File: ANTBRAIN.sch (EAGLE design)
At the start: 26 parts, among them IC1 ATMEGA328P, SW1 SWITCH-SPDTB

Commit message: Shrunk board to 36x36mm
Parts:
- H4: value ICSP -> ICSP2X3-2MM; device pinhead:PINHD-2X3 -> freetronics-jon:ICSP2X3-2MM
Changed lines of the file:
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@@
 <part name="U$5" library="SparkFun" deviceset="5V" device=""/>
 <part name="C6" library="freetronics-master-v1.1" deviceset="CAP" device="0603" value="100nF"/>
-<part name="H4" library="pinhead" deviceset="PINHD-2X3" device="" value="ICSP"/>
 <part name="GND22" library="SparkFun" deviceset="GND" device=""/>
 <part name="U$12" library="SparkFun" deviceset="5V" device=""/>
@@
 <part name="C9" library="freetronics-jon" deviceset="CAP" device="0805" value="10uF"/>
 <part name="U$9" library="SparkFun" deviceset="5V" device=""/>
+<part name="H4" library="freetronics-jon" deviceset="ICSP" device="2X3-2MM"/>
 </parts>
 <sheets>
@@
 <attribute name="VALUE" x="151.384" y="173.101" size="1.778" layer="96"/>
 </instance>
-<instance part="H4" gate="A" x="170.18" y="71.12"/>
 <instance part="GND22" gate="1" x="193.04" y="66.04"/>
 <instance part="U$12" gate="G$1" x="193.04" y="73.66"/>
@@
 </instance>
 <instance part="U$9" gate="G$1" x="215.9" y="76.2"/>
+<instance part="H4" gate="G$1" x="170.18" y="71.12"/>
 </instances>
 <busses>
@@
 </segment>
 <segment>
-<wire x1="175.26" y1="68.58" x2="193.04" y2="68.58" width="0.1524" layer="91"/>
-<pinref part="H4" gate="A" pin="6"/>
+<wire x1="180.34" y1="68.58" x2="193.04" y2="68.58" width="0.1524" layer="91"/>
 <pinref part="GND22" gate="1" pin="GND"/>
 <label x="182.88" y="68.58" size="1.778" layer="95"/>
+<pinref part="H4" gate="G$1" pin="6"/>
 </segment>
 <segment>
@@
 </segment>
 <segment>
-<wire x1="175.26" y1="73.66" x2="193.04" y2="73.66" width="0.1524" layer="91"/>
-<pinref part="H4" gate="A" pin="2"/>
+<wire x1="180.34" y1="73.66" x2="193.04" y2="73.66" width="0.1524" layer="91"/>
 <pinref part="U$12" gate="G$1" pin="5V"/>
 <label x="182.88" y="73.66" size="1.778" layer="95"/>
+<pinref part="H4" gate="G$1" pin="2"/>
 </segment>
 <segment>
@@
 </segment>
 <segment>
-<wire x1="167.64" y1="68.58" x2="147.32" y2="68.58" width="0.1524" layer="91"/>
-<pinref part="H4" gate="A" pin="5"/>
+<wire x1="160.02" y1="68.58" x2="147.32" y2="68.58" width="0.1524" layer="91"/>
 <label x="149.86" y="68.58" size="1.778" layer="95"/>
+<pinref part="H4" gate="G$1" pin="5"/>
 </segment>
 <segment>
@@
 </segment>
 <segment>
-<wire x1="167.64" y1="71.12" x2="147.32" y2="71.12" width="0.1524" layer="91"/>
-<pinref part="H4" gate="A" pin="3"/>
+<wire x1="160.02" y1="71.12" x2="147.32" y2="71.12" width="0.1524" layer="91"/>
 <label x="149.86" y="71.12" size="1.778" layer="95"/>
+<pinref part="H4" gate="G$1" pin="3"/>
 </segment>
 </net>
@@
 </segment>
 <segment>
-<wire x1="167.64" y1="73.66" x2="147.32" y2="73.66" width="0.1524" layer="91"/>
-<pinref part="H4" gate="A" pin="1"/>
+<wire x1="160.02" y1="73.66" x2="147.32" y2="73.66" width="0.1524" layer="91"/>
 <label x="149.86" y="73.66" size="1.778" layer="95"/>
+<pinref part="H4" gate="G$1" pin="1"/>
 </segment>
 </net>
@@
 </segment>
 <segment>
-<wire x1="175.26" y1="71.12" x2="193.04" y2="71.12" width="0.1524" layer="91"/>
-<pinref part="H4" gate="A" pin="4"/>
+<wire x1="180.34" y1="71.12" x2="193.04" y2="71.12" width="0.1524" layer="91"/>
 <label x="182.88" y="71.12" size="1.778" layer="95"/>
-</segment>
-</net>
+<pinref part="H4" gate="G$1" pin="4"/>
+</segment>
+</net>

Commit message: Finished routing for v1.0 release
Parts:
- removed U$2, U$6: L9110SO8, freetronics-jon:L9110SO8
- added IC2, IC3: L9110SO8, freetronics-jon:L9110SO8
- added JP10: POWER, freetronics-jon:M022MM
- added JP8: (no value), freetronics-jon:M022MM
- added JP9: D13, freetronics-jon:M022MM
- added LED2: RED, freetronics-jon:LED0603
- added R2, R3: 10K, freetronics-jon:RESISTOR0603
- added R4: 1K, freetronics-jon:RESISTOR0603
- added R6, R7: 470R, freetronics-jon:RESISTOR0603
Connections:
- removed net N$1: JP2.1, U$2.B
- removed net N$2: JP2.2, U$2.A
- removed net N$3: JP5.2, U$6.B
- removed net N$4: JP5.1, U$6.A
- new net LA: IC2.A, JP2.2
- new net LB: IC2.B, JP2.1
- new net N$5: LED2.A, R4.1
- new net N$6: JP10.1, R7.1
- new net N$8: JP9.1, R6.1
- new net RA: IC3.A, JP5.1
- new net RB: IC3.B, JP5.2
- net 5V: now also R7.2
- net A6: now also R2.2, R3.1
- net D10: now also IC3.OB; no longer U$6.OB
- net D13_SCK: now also R4.2, R6.2
- net D7: now also IC2.OA; no longer U$2.OA
- net D8: now also IC2.OB; no longer U$2.OB
- net D9: now also IC3.OA; no longer U$6.OA
- net GND: now also IC2.GND, IC3.GND, JP10.2, JP9.2, LED2.C, R2.1; no longer U$2.GND, U$6.GND
- net N$9: now also JP8.2
- net VBAT: now also IC2.VCC, IC3.VCC, JP8.1, R3.2; no longer U$2.VCC, U$6.VCC
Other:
- note added: "External LEDs"
- note added: "Flysky Receiver"
- note added: "H-Bridges"
- note added: "Power Supply"
- note added: "https://www.banggood.com/IRangX-Tiny-2_4G-6CH-Flysk-Receiver-Compatible-with-Flysky-PPM-Output-for-Eachine-QX80-QX90-QX95-p-1089802.html"
- note removed: "Front servo control Filter caps https://www.banggood.com/IRangX-Tiny-2_4G-6CH-Flysk-Receiver-Compatible-with-Flysky-PPM-Output-for-Eachine-QX80-QX90-QX95-p-1089802.html"
- moved on the sheet: C2, C3, C6, C8, C9, H3, JP1, JP2, JP3, JP4, JP5, JP7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

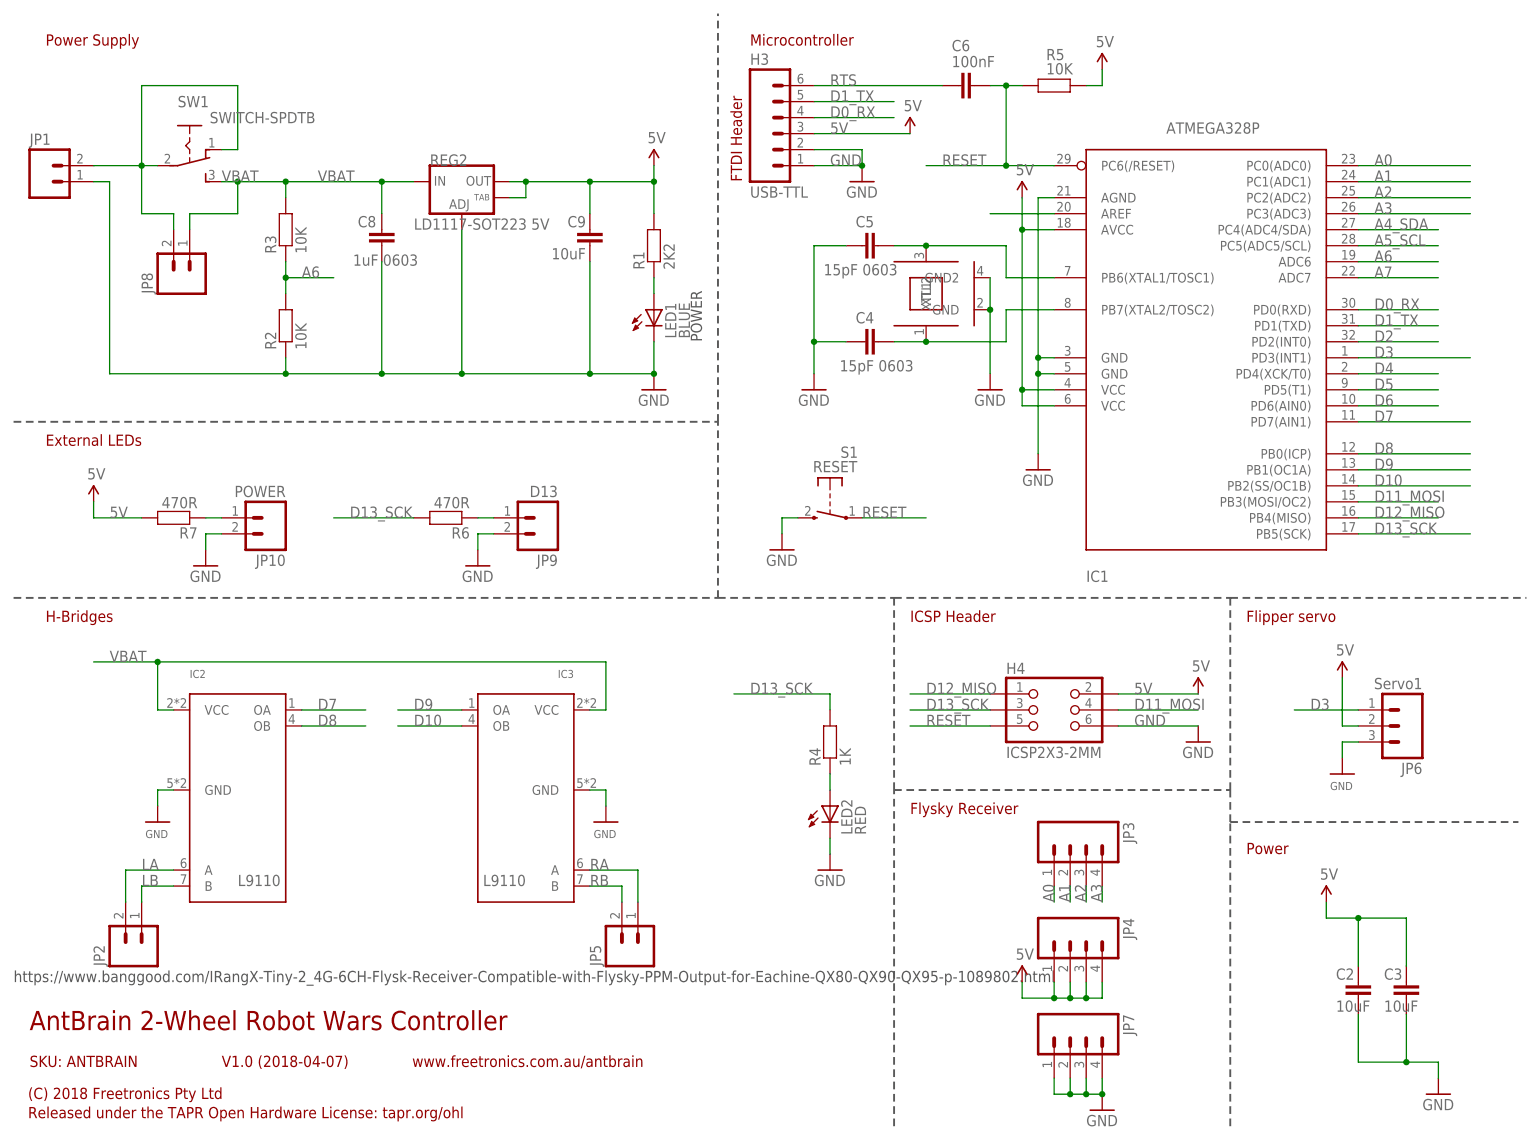
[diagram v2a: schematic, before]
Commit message: Fixed H-Bridge footprints for v1.1 release
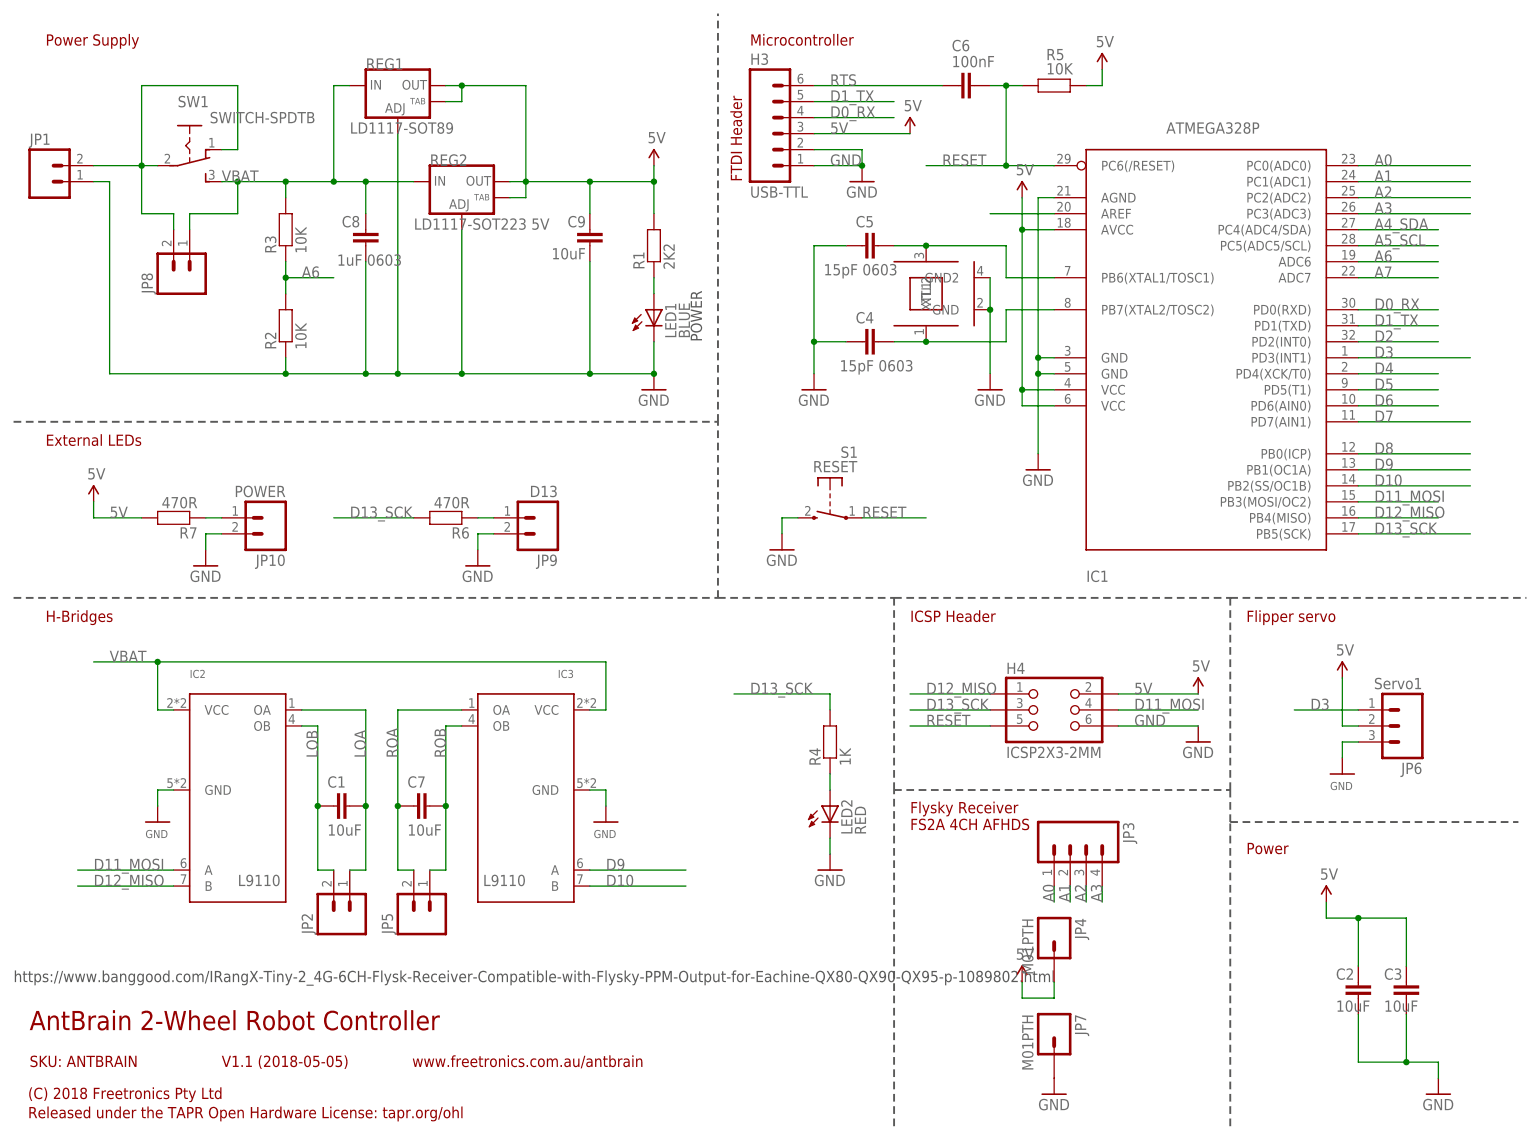
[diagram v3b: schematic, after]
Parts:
- added C1, C7: 10uF, freetronics-jon:CAP0805
- added REG1: LD1117-SOT89, freetronics:V_REG_LM1117SOT89
- JP4, JP7: value (none) -> M01PTH; device freetronics-jon:M04PTH -> freetronics-jon:M01PTH
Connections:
- removed net LA: IC2.A, JP2.2
- removed net LB: IC2.B, JP2.1
- removed net RA: IC3.A, JP5.1
- removed net RB: IC3.B, JP5.2
- new net LOA: C1.1, IC2.OA, JP2.1
- new net LOB: C1.2, IC2.OB, JP2.2
- new net ROA: C7.2, IC3.OA, JP5.2
- new net ROB: C7.1, IC3.OB, JP5.1
- net 5V: now also REG1.OUT, REG1.OUT@1; no longer JP4.2, JP4.3, JP4.4
- net D10: now also IC3.B; no longer IC3.OB
- net D11_MOSI: now also IC2.A
- net D12_MISO: now also IC2.B
- net D7: no longer IC2.OA
- net D8: no longer IC2.OB
- net D9: now also IC3.A; no longer IC3.OA
- net GND: now also REG1.ADJ; no longer JP7.2, JP7.3, JP7.4
- net VBAT: now also REG1.IN
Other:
- note added: "AntBrain 2-Wheel Robot Controller"
- note added: "Flysky Receiver FS2A 4CH AFHDS"
- note added: "V1.1 (2018-05-05)"
- note removed: "AntBrain 2-Wheel Robot Wars Controller"
- note removed: "Flysky Receiver"
- note removed: "V1.0 (2018-04-07)"
- moved on the sheet: C8, JP2, JP5
